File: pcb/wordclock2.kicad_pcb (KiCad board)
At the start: 2 copper layers, 130 x 30 mm, 0 parts

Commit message: progress
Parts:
- added BT1: Battery_Cell, Connect:CR2032H, F.Cu at (161.3, 135.6)
- added BZ1: Buzzer, wordclockFB:PKLCS1212E, F.Cu at (168.1, 88.1)
- added C1: 100u, Capacitors_Tantalum_SMD:CP_Tantalum_Case-D_EIA-7343-31_Hand, F.Cu at (160.8, 99.8)
- added C10: 100n, Capacitors_SMD:C_0805_HandSoldering, F.Cu at (109.5, 100.6)
- added C11: 100n, Capacitors_SMD:C_0805_HandSoldering, F.Cu at (115.1, 90.4)
- added C12: 100n, Capacitors_SMD:C_0805_HandSoldering, F.Cu at (99.1, 96.0)
- added C13: 100n, Capacitors_SMD:C_0805_HandSoldering, F.Cu at (198.6, 103.1)
- added C14: 100n, Capacitors_SMD:C_0805_HandSoldering, F.Cu at (156.2, 104.6)
- added C15: 100n, Capacitors_SMD:C_0805_HandSoldering, F.Cu at (133.3, 101.6)
- added C2: 1u, Capacitors_SMD:C_0805_HandSoldering, F.Cu at (159.5, 81.0)
- added C3: 1u, Capacitors_SMD:C_0805_HandSoldering, F.Cu at (150.9, 88.1)
- added C4: 33p, Capacitors_SMD:C_0805_HandSoldering, F.Cu at (109.2, 86.1)
- added C5: 33p, Capacitors_SMD:C_0805_HandSoldering, F.Cu at (96.0, 86.1)
- added C6: 10u, Capacitors_SMD:C_0805_HandSoldering, F.Cu at (138.2, 94.7)
- added C7: 22p, Capacitors_SMD:C_0805_HandSoldering, F.Cu at (116.8, 81.3)
- added C8: 22p, Capacitors_SMD:C_0805_HandSoldering, F.Cu at (116.8, 85.1)
- added C9: 100n, Capacitors_SMD:C_0805_HandSoldering, F.Cu at (104.6, 86.1)
- added D1: LED, LEDs:LED_0805_HandSoldering, F.Cu at (160.0, 119.4)
- added D2: LED, LEDs:LED_0805_HandSoldering, F.Cu at (116.6, 122.2)
- added D3: DIODE, Diodes_SMD:D_PowerDI-123, F.Cu at (164.6, 96.3)
- added J1: Jack-DC, Connect:BARREL_JACK, F.Cu at (171.7, 96.3)
- added J2: CONN_02X05, wordclockFB:SHF-105-01-L-D-RA, F.Cu at (99.1, 102.6)
- added J3: Micro_SD_Card_Det, wordclockFB:DM3D-SF, F.Cu at (121.9, 108.0)
- added J4: USB_OTG, Connect:USB_Micro-B, F.Cu at (110.5, 105.4)
- added J5: CONN_01X03, wordclockFB:CONN_HEADER_3POS, F.Cu at (202.6, 95.2)
- added J6: CONN_01X03, wordclockFB:CONN_HEADER_3POS, F.Cu at (93.3, 95.2)
- added JP1: Jumper_NO_Small, wordclockFB:SOLDER-JUMPER_1-WAY, F.Cu at (140.5, 98.6)
- added Q1: FDS6890A, Housings_SOIC:SOIC-8_3.9x4.9mm_Pitch1.27mm, F.Cu at (133.3, 83.8)
- added R1: 512, Resistors_SMD:R_0805_HandSoldering, F.Cu at (113.3, 96.0)
- added R10: 10k, Resistors_SMD:R_0805_HandSoldering, F.Cu at (198.9, 96.3)
- added R11: 10k, Resistors_SMD:R_0805_HandSoldering, F.Cu at (200.4, 103.1)
- added R12: 1k, Resistors_SMD:R_0805_HandSoldering, F.Cu at (164.8, 81.0)
- added R13: 10k, Resistors_SMD:R_0805_HandSoldering, F.Cu at (133.3, 103.6)
- added R14: 10k, Resistors_SMD:R_0805_HandSoldering, F.Cu at (162.1, 103.1)
- added R15: 10k, Resistors_SMD:R_0805_HandSoldering, F.Cu at (176.8, 93.7)
- added R2: 512, Resistors_SMD:R_0805_HandSoldering, F.Cu at (130.8, 127.0)
- added R3: 10k, Resistors_SMD:R_0805_HandSoldering, F.Cu at (158.5, 87.6)
- added R4: 10k, Resistors_SMD:R_0805_HandSoldering, F.Cu at (115.1, 92.5)
- added R5: 10k, Resistors_SMD:R_0805_HandSoldering, F.Cu at (98.8, 90.9)
- added R6: 10k, Resistors_SMD:R_0805_HandSoldering, F.Cu at (148.1, 91.4)
- added R7: 10k, Resistors_SMD:R_0805_HandSoldering, F.Cu at (148.1, 84.8)
- added R8: 10k, Resistors_SMD:R_0805_HandSoldering, F.Cu at (177.8, 88.1)
- added R9: 10k, Resistors_SMD:R_0805_HandSoldering, F.Cu at (176.8, 91.7)
- added SW1: SW_Push, Buttons_Switches_SMD:SW_SPST_KMR2, F.Cu at (123.4, 90.2)
- added SW2: SW_Push, Buttons_Switches_ThroughHole:SW_Tactile_SPST_Angled_PTS645Vx39-2LFS, F.Cu at (135.6, 106.7)
- added SW3: SW_Push, Buttons_Switches_ThroughHole:SW_Tactile_SPST_Angled_PTS645Vx39-2LFS, F.Cu at (164.3, 106.7)
- added SW4: SW_Push, Buttons_Switches_SMD:SW_SPST_KMR2, F.Cu at (200.7, 107.7)
- added SW5: SW_Push, Buttons_Switches_SMD:SW_SPST_KMR2, F.Cu at (123.4, 94.0)
- added SW6: SW_Push, Buttons_Switches_SMD:SW_SPST_KMR2, F.Cu at (178.1, 82.0)
- added U1: MAXIM_MAX44009, wordclockFB:MAX44009, F.Cu at (148.1, 88.1)
- added U2: Si7021, wordclockFB:Si7021-A20, F.Cu at (159.5, 83.6)
- added U3: TPS77833_SO8, Housings_SOIC:SOIC-8_3.9x4.9mm_Pitch1.27mm, F.Cu at (133.3, 92.7)
- added U4: STM32L433CCT6, Housings_QFP:LQFP-48_7x7mm_Pitch0.5mm, F.Cu at (106.7, 93.2)
- added U5: ESP-12E, ESP8266:ESP-12E_SMD, F.Cu at (195.3, 101.6)
- added Y1: 8MHz, Crystals:Crystal_SMD_HC49-SD_HandSoldering, F.Cu at (102.9, 82.5)
- added Y2: 32.768kHz, Crystals:Crystal_SMD_SeikoEpson_MC306-4pin_8.0x3.2mm_HandSoldering, F.Cu at (123.7, 84.1)

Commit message: progress
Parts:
- added C16: 100n, Capacitors_SMD:C_0805_HandSoldering, F.Cu at (101.6, 86.1)
- moved D1 49.3 mm to (117.3, 94.7), turned to 180 degrees
- moved R2 37.5 mm to (104.9, 99.8)
- moved D2 23.4 mm to (104.9, 101.9), turned to 180 degrees
- moved C4 1.78 mm to (111.0, 86.1)
- moved C9 1.65 mm to (106.3, 86.1)
- moved C5 0.89 mm to (96.9, 86.1)
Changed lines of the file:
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@@
 (kicad_pcb (version 4) (host pcbnew 4.0.7-e2-6376~58~ubuntu14.04.1)
   (general
-    (links 162)
-    (no_connects 162)
+    (links 164)
+    (no_connects 164)
     (area 82.924999 79.924999 213.075001 110.075001)
     (thickness 1.6)
@@
     (tracks 0)
     (zones 0)
-    (modules 56)
+    (modules 57)
     (nets 70)
   )
@@
   )
   (module Capacitors_SMD:C_0805_HandSoldering (layer F.Cu)
-    (at 109.22 86.106 180)
+    (at 110.998 86.106 180)
     (descr "Capacitor SMD 0805, hand soldering")
     (tags "capacitor 0805")
@@
   )
   (module Capacitors_SMD:C_0805_HandSoldering (layer F.Cu)
-    (at 96.012 86.106)
+    (at 96.901 86.106)
     (descr "Capacitor SMD 0805, hand soldering")
     (tags "capacitor 0805")
@@
   )
   (module Capacitors_SMD:C_0805_HandSoldering (layer F.Cu)
-    (at 104.648 86.106 180)
+    (at 106.299 86.106 180)
     (descr "Capacitor SMD 0805, hand soldering")
     (tags "capacitor 0805")
@@
   )
   (module LEDs:LED_0805_HandSoldering (layer F.Cu)
-    (at 160.02 119.38 270)
+    (at 117.348 94.742 180)
     (descr "Resistor SMD 0805, hand soldering")
     (tags "resistor 0805")
     (attr smd)
-    (fp_text reference D1 (at 0 -1.7 270) (layer F.SilkS)
-      (effects (font (size 1 1) (thickness 0.15)))
-    )
-    (fp_text value LED (at 0 1.75 270) (layer F.Fab)
+    (fp_text reference D1 (at 0 -1.7 180) (layer F.SilkS)
+      (effects (font (size 1 1) (thickness 0.15)))
+    )
+    (fp_text value LED (at 0 1.75 180) (layer F.Fab)
       (effects (font (size 1 1) (thickness 0.15)))
     )
@@
     (fp_line (start 2.35 0.9) (end -2.35 0.9) (layer F.CrtYd) (width 0.05))
     (fp_line (start -2.2 -0.75) (end -2.2 0.75) (layer F.SilkS) (width 0.12))
-    (pad 1 smd rect (at -1.35 0 270) (size 1.5 1.3) (layers F.Cu F.Paste F.Mask)
-      (net 1 GND))
-    (pad 2 smd rect (at 1.35 0 270) (size 1.5 1.3) (layers F.Cu F.Paste F.Mask)
+    (pad 1 smd rect (at -1.35 0 180) (size 1.5 1.3) (layers F.Cu F.Paste F.Mask)
+      (net 1 GND))
+    (pad 2 smd rect (at 1.35 0 180) (size 1.5 1.3) (layers F.Cu F.Paste F.Mask)
       (net 13 "Net-(D1-Pad2)"))
     (model ${KISYS3DMOD}/LEDs.3dshapes/LED_0805.wrl
@@
   )
   (module LEDs:LED_0805_HandSoldering (layer F.Cu)
-    (at 116.586 122.174 270)
+    (at 104.902 101.854 180)
     (descr "Resistor SMD 0805, hand soldering")
     (tags "resistor 0805")
     (attr smd)
-    (fp_text reference D2 (at 0 -1.7 270) (layer F.SilkS)
-      (effects (font (size 1 1) (thickness 0.15)))
-    )
-    (fp_text value LED (at 0 1.75 270) (layer F.Fab)
+    (fp_text reference D2 (at 0 -1.7 180) (layer F.SilkS)
+      (effects (font (size 1 1) (thickness 0.15)))
+    )
+    (fp_text value LED (at 0 1.75 180) (layer F.Fab)
       (effects (font (size 1 1) (thickness 0.15)))
     )
@@
     (fp_line (start 2.35 0.9) (end -2.35 0.9) (layer F.CrtYd) (width 0.05))
     (fp_line (start -2.2 -0.75) (end -2.2 0.75) (layer F.SilkS) (width 0.12))
-    (pad 1 smd rect (at -1.35 0 270) (size 1.5 1.3) (layers F.Cu F.Paste F.Mask)
-      (net 1 GND))
-    (pad 2 smd rect (at 1.35 0 270) (size 1.5 1.3) (layers F.Cu F.Paste F.Mask)
+    (pad 1 smd rect (at -1.35 0 180) (size 1.5 1.3) (layers F.Cu F.Paste F.Mask)
+      (net 1 GND))
+    (pad 2 smd rect (at 1.35 0 180) (size 1.5 1.3) (layers F.Cu F.Paste F.Mask)
       (net 14 "Net-(D2-Pad2)"))
     (model ${KISYS3DMOD}/LEDs.3dshapes/LED_0805.wrl
@@
   )
   (module Resistors_SMD:R_0805_HandSoldering (layer F.Cu)
-    (at 130.81 127)
+    (at 104.902 99.822)
     (descr "Resistor SMD 0805, hand soldering")
     (tags "resistor 0805")
@@
       (at (xyz 0 0 0))
       (scale (xyz 1 1 1))
+      (rotate (xyz 0 0 0))
+    )
+  )
+  (module Capacitors_SMD:C_0805_HandSoldering (layer F.Cu)
+    (at 101.6 86.106 180)
+    (descr "Capacitor SMD 0805, hand soldering")
+    (tags "capacitor 0805")
+    (attr smd)
+    (fp_text reference C16 (at 0 -1.75 180) (layer F.SilkS)
+      (effects (font (size 1 1) (thickness 0.15)))
+    )
+    (fp_text value 100n (at 0 1.75 180) (layer F.Fab)
+      (effects (font (size 1 1) (thickness 0.15)))
+    )
+    (fp_text user %R (at 0 -1.75 180) (layer F.Fab)
+      (effects (font (size 1 1) (thickness 0.15)))
+    )
+    (fp_line (start -1 0.62) (end -1 -0.62) (layer F.Fab) (width 0.1))
+    (fp_line (start 1 0.62) (end -1 0.62) (layer F.Fab) (width 0.1))
+    (fp_line (start 1 -0.62) (end 1 0.62) (layer F.Fab) (width 0.1))
+    (fp_line (start -1 -0.62) (end 1 -0.62) (layer F.Fab) (width 0.1))
+    (fp_line (start 0.5 -0.85) (end -0.5 -0.85) (layer F.SilkS) (width 0.12))
+    (fp_line (start -0.5 0.85) (end 0.5 0.85) (layer F.SilkS) (width 0.12))
+    (fp_line (start -2.25 -0.88) (end 2.25 -0.88) (layer F.CrtYd) (width 0.05))
+    (fp_line (start -2.25 -0.88) (end -2.25 0.87) (layer F.CrtYd) (width 0.05))
+    (fp_line (start 2.25 0.87) (end 2.25 -0.88) (layer F.CrtYd) (width 0.05))
+    (fp_line (start 2.25 0.87) (end -2.25 0.87) (layer F.CrtYd) (width 0.05))
+    (pad 1 smd rect (at -1.25 0 180) (size 1.5 1.25) (layers F.Cu F.Paste F.Mask)
+      (net 3 +3V3))
+    (pad 2 smd rect (at 1.25 0 180) (size 1.5 1.25) (layers F.Cu F.Paste F.Mask)
+      (net 1 GND))
+    (model Capacitors_SMD.3dshapes/C_0805.wrl
+      (at (xyz 0 0 0))
+      (scale (xyz 1 1 1))

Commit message: progress
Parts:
- moved C2 35.2 mm to (129.8, 99.8), turned to 270 degrees
- moved U2 30.6 mm to (133.0, 98.8), turned to 180 degrees
- moved J4 25.7 mm to (136.1, 107.2)
- moved SW4 25.6 mm to (199.1, 82.2), turned to 180 degrees
- moved R13 23.0 mm to (110.4, 104.1), turned to 0 degrees
- moved SW2 23.0 mm to (112.6, 106.7)
- moved C15 20.6 mm to (112.8, 101.2), turned to 0 degrees
- moved R9 18.4 mm to (192.7, 82.3), turned to 270 degrees
- moved R15 16.4 mm to (188.6, 82.3), turned to 270 degrees
- moved R8 14.1 mm to (190.6, 82.3)
- moved R3 13.5 mm to (145.0, 88.1)
- moved C14 9.65 mm to (165.2, 101.2), turned to 180 degrees
- moved R10 9.37 mm to (200.9, 87.1)
- moved C1 8.91 mm to (160.1, 90.9), turned to 90 degrees
- moved SW6 6.10 mm to (184.2, 81.9)
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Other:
- outline, holes or cut-outs redrawn

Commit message: battery
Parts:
- BT1: footprint Connect:CR2032H -> wordclockFB:LR44
- moved BT1 34.1 mm to (150.7, 103.3)
- moved U2 3.76 mm to (136.7, 99.6)
- moved C2 3.06 mm to (132.8, 100.1)
- moved U3 1.78 mm to (132.1, 90.3)
- moved JP1 0.99 mm to (136.4, 94.5), turned to 0 degrees
- moved C6 0.52 mm to (137.4, 90.7)
- moved C10 0.13 mm to (109.5, 100.7)
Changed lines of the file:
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@@
 (kicad_pcb (version 4) (host pcbnew 4.0.7-e2-6376~58~ubuntu14.04.1)
   (general
-    (links 164)
-    (no_connects 164)
-    (area 80.178 78.025 215.832 149.411)
+    (links 165)
+    (no_connects 165)
+    (area 82.924999 79.924999 213.075001 110.075001)
     (thickness 1.6)
     (drawings 12)
@@
     )
   )
-  (module Connect:CR2032H (layer F.Cu)
-    (at 161.29 135.636)
-    (fp_text reference BT1 (at -15.24 -12.7) (layer F.SilkS)
-      (effects (font (size 1 1) (thickness 0.15)))
-    )
-    (fp_text value Battery_Cell (at -15.24 12.7) (layer F.Fab)
-      (effects (font (size 1 1) (thickness 0.15)))
-    )
-    (fp_line (start -4.49 -3.8) (end 3.06 -3.8) (layer F.CrtYd) (width 0.05))
-    (fp_line (start 3.06 -3.8) (end 3.06 3.65) (layer F.CrtYd) (width 0.05))
-    (fp_line (start 3.06 3.65) (end -4.44 3.65) (layer F.CrtYd) (width 0.05))
-    (fp_line (start -4.69 -3.3) (end 2.66 -3.3) (layer F.SilkS) (width 0.12))
-    (fp_line (start 2.66 -3.3) (end 2.66 3.3) (layer F.SilkS) (width 0.12))
-    (fp_line (start 2.66 3.3) (end -4.69 3.3) (layer F.SilkS) (width 0.12))
-    (fp_line (start 0 3.81) (end 0 5.08) (layer F.SilkS) (width 0.12))
-    (fp_line (start -0.63 4.45) (end 0.63 4.45) (layer F.SilkS) (width 0.12))
-    (fp_line (start -4.45 -2.54) (end 1.9 -2.54) (layer F.Fab) (width 0.1))
-    (fp_line (start 1.9 -2.54) (end 1.9 2.54) (layer F.Fab) (width 0.1))
-    (fp_line (start 1.9 2.54) (end -4.45 2.54) (layer F.Fab) (width 0.1))
-    (fp_line (start 1.9 -3.17) (end 2.54 -3.17) (layer F.Fab) (width 0.1))
-    (fp_line (start 2.54 -3.17) (end 2.54 3.17) (layer F.Fab) (width 0.1))
-    (fp_line (start 2.54 3.17) (end 1.9 3.17) (layer F.Fab) (width 0.1))
-    (fp_line (start 0.63 -3.17) (end 1.9 -3.17) (layer F.Fab) (width 0.1))
-    (fp_line (start 1.9 3.17) (end -4.45 3.17) (layer F.Fab) (width 0.1))
-    (fp_line (start -4.45 -3.17) (end 0.63 -3.17) (layer F.Fab) (width 0.1))
-    (fp_circle (center -15.24 0) (end -16.51 -8.89) (layer F.Fab) (width 0.1))
-    (fp_circle (center -15.24 0) (end -8.89 8.89) (layer F.Fab) (width 0.1))
-    (fp_arc (start -15.24 0) (end -4.44 3.65) (angle 322) (layer F.CrtYd) (width 0.05))
-    (fp_arc (start -15.24 0) (end -4.69 3.3) (angle 325) (layer F.SilkS) (width 0.12))
-    (pad 2 thru_hole circle (at -22.86 0) (size 2.29 2.29) (drill 1.02) (layers *.Cu *.Mask)
-      (net 1 GND))
-    (pad 1 thru_hole circle (at 0 0) (size 2.29 2.29) (drill 1.02) (layers *.Cu *.Mask)
-      (net 2 "Net-(BT1-Pad1)"))
-  )
   (module wordclockFB:PKLCS1212E (layer F.Cu)
     (at 172.847 88.011)
@@
   )
   (module Capacitors_SMD:C_0805_HandSoldering (layer F.Cu)
-    (at 129.794 99.822 270)
+    (at 132.842 100.076 270)
     (descr "Capacitor SMD 0805, hand soldering")
     (tags "capacitor 0805")
@@
   )
   (module Capacitors_SMD:C_0805_HandSoldering (layer F.Cu)
-    (at 136.906 90.805 270)
+    (at 137.414 90.678 270)
     (descr "Capacitor SMD 0805, hand soldering")
     (tags "capacitor 0805")
@@
   )
   (module Capacitors_SMD:C_0805_HandSoldering (layer F.Cu)
-    (at 109.474 100.584 270)
+    (at 109.474 100.711 270)
     (descr "Capacitor SMD 0805, hand soldering")
     (tags "capacitor 0805")
@@
   )
   (module wordclockFB:SOLDER-JUMPER_1-WAY (layer F.Cu)
-    (at 137.16 95.123 270)
-    (fp_text reference JP1 (at 0 1.905 270) (layer F.SilkS)
+    (at 136.398 94.488)
+    (fp_text reference JP1 (at 0 1.905) (layer F.SilkS)
       (effects (font (size 0.762 0.762) (thickness 0.1524)))
     )
-    (fp_text value Jumper_NO_Small (at 0 0 270) (layer F.SilkS) hide
+    (fp_text value Jumper_NO_Small (at 0 0) (layer F.SilkS) hide
       (effects (font (size 0.762 0.762) (thickness 0.1524)))
     )
@@
     (fp_arc (start -0.254 0) (end -1.27 0) (angle 90) (layer F.SilkS) (width 0.2032))
     (fp_arc (start -0.254 0) (end -0.254 1.016) (angle 90) (layer F.SilkS) (width 0.2032))
-    (pad 1 smd rect (at -0.65 0 270) (size 1 1) (layers F.Cu F.Paste F.Mask)
-      (net 3 +3V3))
-    (pad 2 smd rect (at 0.65 0 270) (size 1 1) (layers F.Cu F.Paste F.Mask)
+    (pad 1 smd rect (at -0.65 0) (size 1 1) (layers F.Cu F.Paste F.Mask)
+      (net 3 +3V3))
+    (pad 2 smd rect (at 0.65 0) (size 1 1) (layers F.Cu F.Paste F.Mask)
       (net 2 "Net-(BT1-Pad1)"))
   )
@@
   )
   (module wordclockFB:Si7021-A20 (layer F.Cu)
-    (at 132.969 98.806 180)
+    (at 136.652 99.568 180)
     (fp_text reference U2 (at 0 3.5 180) (layer F.SilkS)
       (effects (font (size 1 1) (thickness 0.15)))
@@
   )
   (module Housings_SOIC:SOIC-8_3.9x4.9mm_Pitch1.27mm (layer F.Cu)
-    (at 132.08 88.519)
+    (at 132.08 90.297)
     (descr "8-Lead Plastic Small Outline (SN) - Narrow, 3.90 mm Body [SOIC] (see Microchip Packaging Specification 00000049BS.pdf)")
     (tags "SOIC 1.27")
@@
     )
   )
+  (module wordclockFB:LR44 (layer F.Cu)
+    (at 150.749 103.251)
+    (fp_text reference BT1 (at 0.254 -7.366) (layer F.SilkS)
+      (effects (font (size 1 1) (thickness 0.15)))
+    )
+    (fp_text value Battery_Cell (at 0 7.874) (layer F.Fab)
+      (effects (font (size 1 1) (thickness 0.15)))
+    )
+    (fp_line (start -6.605 -6.07) (end -6.605 6.07) (layer F.Fab) (width 0.15))
+    (fp_line (start -6.605 6.07) (end 6.605 6.07) (layer F.Fab) (width 0.15))
+    (fp_line (start 6.605 6.07) (end 6.605 -6.07) (layer F.Fab) (width 0.15))
+    (fp_line (start 6.605 -6.07) (end -6.605 -6.07) (layer F.Fab) (width 0.15))
+    (pad 1 thru_hole circle (at -6.605 0) (size 3 3) (drill 1.8) (layers *.Cu *.Mask)
+      (net 2 "Net-(BT1-Pad1)"))
+    (pad 1 thru_hole circle (at 6.605 0) (size 3 3) (drill 1.8) (layers *.Cu *.Mask)
+      (net 2 "Net-(BT1-Pad1)"))
+    (pad 2 smd rect (at 0 0) (size 4 4) (layers F.Cu F.Paste F.Mask)
+      (net 1 GND))
+  )
   (gr_line (start 156.6 97) (end 156.6 80) (angle 90) (layer Edge.Cuts) (width 0.15))

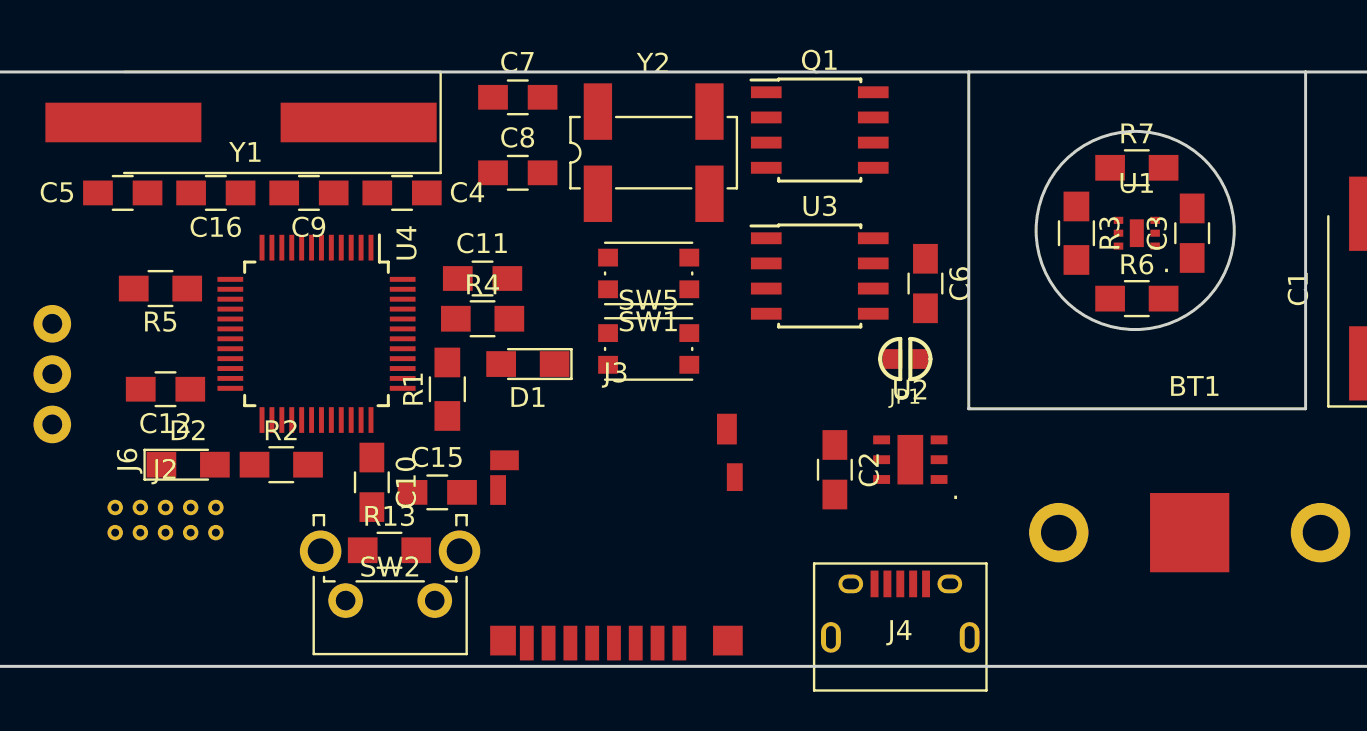
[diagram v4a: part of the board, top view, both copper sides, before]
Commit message: progress, added 32kHz Crystal datasheet
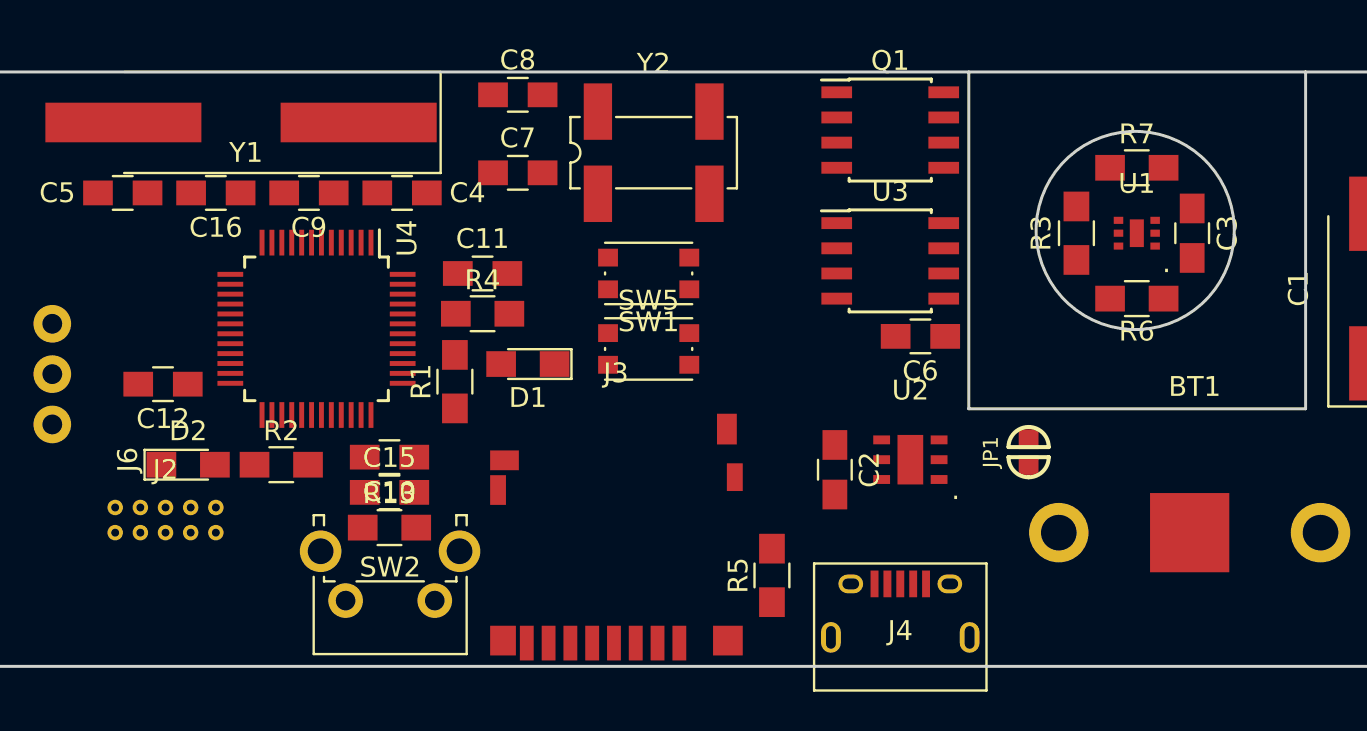
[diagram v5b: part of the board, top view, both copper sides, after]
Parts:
- C3: value 1u -> 100n
- Y2: value 32.768kHz -> Crystal_GND23
- moved R5 34.1 mm to (129.7, 105.4), turned to 90 degrees
- moved JP1 7.80 mm to (142.6, 99.2), turned to 270 degrees
- moved C8 3.94 mm to (116.8, 81.2)
- moved C7 3.81 mm to (116.8, 85.1)
- moved U3 3.64 mm to (135.6, 89.5)
- moved Q1 3.56 mm to (135.6, 82.9)
- moved C6 2.68 mm to (137.2, 93.3), turned to 180 degrees
- moved C15 2.41 mm to (110.4, 101.2)
- moved C10 1.55 mm to (110.4, 99.4), turned to 180 degrees
- moved R13 1.14 mm to (110.4, 103.0)
- moved R1 0.54 mm to (113.7, 95.6)
- moved C12 0.28 mm to (98.9, 95.8)
- moved C11 0.25 mm to (115.1, 90.2)
- moved R4 0.25 mm to (115.1, 92.2)
- moved U4 0.25 mm to (106.7, 93.0)
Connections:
- Y2 pad 2: Net-(C8-Pad2) -> Net-(Y2-Pad2)
- Y2 pad 3: (no net) -> Net-(Y2-Pad3)
- Y2 pad 4: (no net) -> Net-(C8-Pad2)
